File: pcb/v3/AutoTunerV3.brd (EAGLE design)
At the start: 100 x 80 mm, 113 parts, among them IC2 317EMP, Q1 32,768kHz, Q2 BSS123, Q3 BSS84, U1 TPS63070RNMR, Y1 8MHz

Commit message: board v3 improvements
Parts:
- added D1: (no value), diode:SOD323-R
- R32: value 100 -> 60
- moved T1 3.91 mm to (41.7, 55.8), turned to 0 degrees
- moved R28 3.25 mm to (44.7, 55.7), turned to 270 degrees
- moved ST_LINK 1.27 mm to (97.6, 56.4)
- moved +5V 0.95 mm to (33.6, 59.2)
- moved BUZZER 0.95 mm to (41.0, 47.1)
- moved JP2 0.95 mm to (97.6, 68.1)
- moved C10 0.64 mm to (55.3, 59.4)
- moved C11 0.64 mm to (55.3, 53.1)
- moved R37 0.64 mm to (54.3, 56.3)
- moved Q1 0.63 mm to (56.5, 56.3)
- moved R34 0.58 mm to (36.4, 56.0), turned to 90 degrees
- moved VBAT 0.32 mm to (7.60, 68.4)
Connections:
- net N$54: now also D1.A
- net N$55: now also D1.C
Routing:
- net GND: track 325.5 -> 340.0 mm, vias 16 -> 21
- net N$54: track 7.12 -> 13.5 mm
- net BUZZER: track 35.3 -> 29.3 mm
- net +3V3: track 170.2 -> 173.7 mm
- net N$55: track 7.98 -> 10.2 mm
- net N$56: track 4.19 -> 2.06 mm
- net +5V: track 26.8 -> 25.4 mm
- net SWDIO: track 22.5 -> 23.7 mm
- net SWDCLK: track 24.3 -> 25.6 mm
- net N$50: track 20.1 -> 21.0 mm
- net N$49: track 22.5 -> 23.5 mm
- net N$48: track 25.4 -> 26.4 mm
- net N$39: track 27.6 -> 28.5 mm
- net OSC32OUT: track 10.7 -> 11.3 mm
- net OSC32IN: track 12.7 -> 12.2 mm
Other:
- board text added: "+ -"
- board text added: "+3V3"
- board text added: "+5V"
- board text added: "BuildInLED"
- board text added: "Extenions"
- board text added: "GND"
- board text added: "Input"
- board text added: "SIGNAL_IN"
- board text added: "SIGNAL_OPAMP"
- board text added: "VBAT"
- board text added: "VBUS"
- board text added: "microcontroller"
- board text removed: "-"
- board text removed: "A_IN"
- board text removed: "PC13"
- board text removed: "uC"

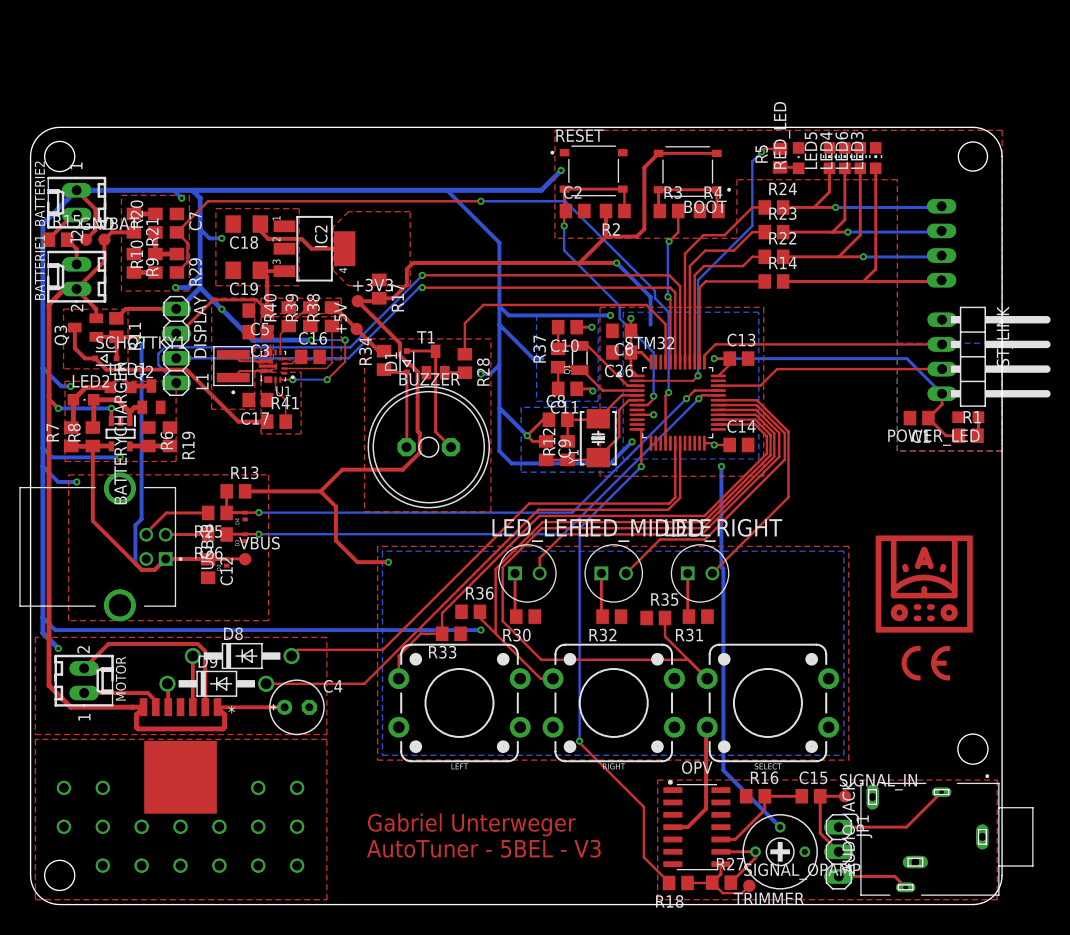
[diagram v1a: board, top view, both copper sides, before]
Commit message: board v3 dcdc design change
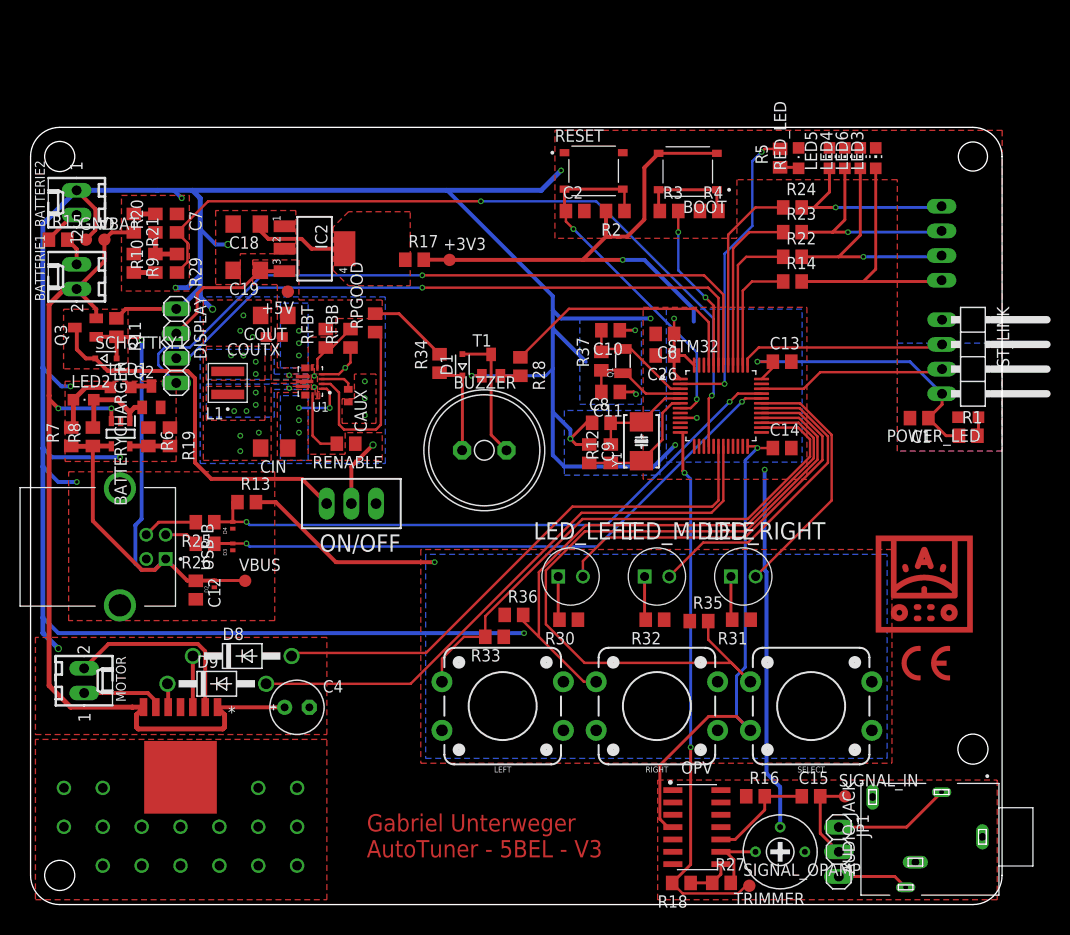
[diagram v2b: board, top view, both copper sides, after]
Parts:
- removed C16: 100n, rcl:C0805
- removed C17, C5: 47u, rcl:C0805
- removed C3: 10u, rcl:C0805
- removed R38, R39: 100k, rcl:R0805
- removed R40: 523k, rcl:R0805
- removed R41: 10k, rcl:R0805
- added CAUX: 100n, rcl:C0402
- added CIN, COUT: 47u, rcl:C1206
- added COUTX: 10u, rcl:C0603
- added ON/OFF: (no value), switch:TL3XPO
- added RENABLE: 10k, rcl:R0805
- added RFBB, RPGOOD: 100k, rcl:R0805
- added RFBT: 523k, rcl:R0805
- moved +3V3 10.4 mm to (43.1, 66.4)
- moved +5V 8.06 mm to (26.5, 63.1), turned to 180 degrees
- moved D1 5.72 mm to (44.5, 55.6)
- moved BUZZER 5.72 mm to (46.7, 46.8)
- moved R28 5.72 mm to (50.4, 55.4)
- moved R34 5.72 mm to (42.1, 55.7)
- moved T1 5.72 mm to (47.4, 55.5)
- moved R17 4.72 mm to (39.5, 66.4), turned to 0 degrees
- moved C26 4.46 mm to (65.3, 56.5)
- moved C6 4.46 mm to (65.3, 58.7)
- moved R35 4.46 mm to (68.8, 29.2)
- moved STM32 4.46 mm to (71.1, 51.3)
- moved C13 4.46 mm to (77.4, 55.9)
- moved C14 4.46 mm to (77.4, 47.0)
- moved C10 4.46 mm to (59.7, 59.1)
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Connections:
- net N$58 renamed L2
- net N$59 renamed L1
- removed net N$45: R18.2, STM32.12
- new net N$3: ON/OFF.3, Q3.3, SCHOTTKY1.C
- new net N$7: OPV.8, R18.1, R27.1
- net +5V: now also COUT.1, COUTX.1, RFBT.2, RPGOOD.2; no longer C3.1, C5.1, R38.2, R40.2
- net GND: now also CAUX.2, CIN.2, COUT.2, COUTX.2, RFBB.1; no longer C16.2, C17.2, C3.2, C5.2, R39.1
- net N$60: now also CAUX.1; no longer C16.1
- net N$61: now also RPGOOD.1; no longer R38.1
- net N$62: now also RFBB.2, RFBT.1; no longer R39.2, R40.1
- net N$64: now also RENABLE.2; no longer R41.2
- net SIGNAL_OPAMP: now also R18.2, STM32.12; no longer OPV.8, R18.1, R27.1
- net VIN: now also CIN.1, ON/OFF.2, RENABLE.1; no longer C17.1, Q3.3, R41.1, SCHOTTKY1.C
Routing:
- net N$45: track 53.6 -> 0.00 mm, vias 2 -> 0
- net SIGNAL_OPAMP: track 9.41 -> 56.5 mm, vias 0 -> 2
- net N$3: track 0.00 -> 39.7 mm
- net VIN: track 25.1 -> 12.8 mm, vias 0 -> 5
- net N$61: track 8.93 -> 20.0 mm
- net GND: track 340.0 -> 330.2 mm, vias 21 -> 29
- net USB+: track 58.0 -> 64.6 mm
- net USB-: track 56.5 -> 62.8 mm
- net N$7: track 0.00 -> 4.53 mm
- net DISPLAY_SDA: track 61.7 -> 66.2 mm
- net SWDCLK: track 25.6 -> 21.3 mm
- net MOTOR_PWM2: track 56.2 -> 60.5 mm
- net SWDIO: track 23.7 -> 19.4 mm
- net MOTOR_PWM1: track 51.8 -> 56.1 mm
- net DISPLAY_SCL: track 69.1 -> 73.4 mm
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- added copper zone on layer 16, net +5V
- added copper zone on layer 1, net L1
- added copper zone on layer 16, net L1
- added copper zone on layer 1, net L2
- added copper zone on layer 16, net L2
- added copper zone on layer 16, net VIN
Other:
- board text removed: "DCDC"

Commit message: board v3 finished
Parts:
- removed LED5, LED6: (no value), led:CHIP-LED0805
- added LED_CHARGE_GREEN, LED_CHARGE_RED: (no value), led:CHIPLED_0805
- LED1, LED2: device led:CHIPLED_0805 -> led:CHIP-LED0805
- R32: value 60 -> 56
- moved LED2 83.7 mm to (85.4, 76.8), turned to 0 degrees
- moved LED1 81.2 mm to (87.0, 76.8), turned to 0 degrees
- moved LED3 3.18 mm to (83.8, 76.8)
- moved LED4 1.59 mm to (82.2, 76.8)
- moved VBAT 0.32 mm to (7.92, 68.4)
- moved BATTERIE1 0.32 mm to (5.06, 64.6)
- moved BATTERIE2 0.32 mm to (5.06, 72.2)
- moved GND 0.32 mm to (6.01, 68.4)
- moved R15 0.32 mm to (3.15, 68.4)
- renumbered C4 to C_H-BRIDGE, D8 to D_H-BRIDGE1, D9 to D_H-BRIDGE2, JP2 to EXTENSIONS, Q1 to QUARTZ2, Q2 to N-CHANNEL, Q3 to P-CHANNEL, RED_LED to LED_INDICATOR, T1 to NPN, Y1 to QUARTZ
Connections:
- net GND: now also LED1.C, LED2.C; no longer LED5.C, LED6.C
- net N$11: now also LED_CHARGE_GREEN.A, LED_CHARGE_RED.A; no longer LED1.A, LED2.A
- net N$12: now also LED_CHARGE_GREEN.C; no longer LED1.C
- net N$39: now also LED1.A; no longer LED3.A
- net N$48: now also LED2.A; no longer LED6.A
- net N$49: now also LED3.A; no longer LED4.A
- net N$50: now also LED4.A; no longer LED5.A
- net N$9: now also LED_CHARGE_RED.C; no longer LED2.C
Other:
- board text added: "AutoTuner V3 - Maturaprojekt Gabriel Unterweger - 5BEL TFO Meran 23 / 24"
- board text removed: "Gabriel Unterweger AutoTuner - 5BEL - V3"

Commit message: settings menu
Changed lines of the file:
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@@
 <drawing>
 <settings>
-<setting alwaysvectorfont="yes"/>
+<setting alwaysvectorfont="no"/>
 <setting verticaltext="up"/>
 </settings>
@@
 <attribute name="VALUE" x="79.675" y="11.035" size="1.27" layer="27" rot="R180"/>
 </element>
-<element name="JP1" library="pinhead" library_urn="urn:adsk.eagle:library:325" package="1X03" package3d_urn="urn:adsk.eagle:package:22458/2" value="" x="83.1925" y="5.43" smashed="yes" rot="R270">
-<attribute name="NAME" x="85.0213" y="9.3162" size="1.27" layer="25" ratio="10" rot="R270"/>
-<attribute name="POPULARITY" value="92" x="83.1925" y="5.43" size="1.778" layer="27" rot="R270" display="off"/>
-<attribute name="VALUE" x="80.0175" y="9.24" size="1.27" layer="27" rot="R270"/>
-</element>
 <element name="LED1" library="led" library_urn="urn:adsk.eagle:library:259" package="CHIP-LED0805" package3d_urn="urn:adsk.eagle:package:15818/2" value="" x="86.995" y="76.835" smashed="yes">
 <attribute name="LCSC_PART" value="C2297" x="86.995" y="76.835" size="1.778" layer="27" display="off"/>
@@
 <attribute name="VALUE" x="25.7175" y="60.325" size="1.27" layer="27" rot="R180"/>
 </element>
+<element name="JP1" library="pinhead" library_urn="urn:adsk.eagle:library:325" package="1X03" package3d_urn="urn:adsk.eagle:package:22458/2" value="" x="83.185" y="5.3975" smashed="yes" rot="R270">
+<attribute name="NAME" x="85.0138" y="9.2837" size="1.27" layer="25" ratio="10" rot="R270"/>
+<attribute name="POPULARITY" value="92" x="83.185" y="5.3975" size="1.778" layer="27" rot="R270" display="off"/>
+<attribute name="VALUE" x="80.01" y="9.2075" size="1.27" layer="27" rot="R270"/>
+</element>
 </elements>
 <signals>
@@
 <signal name="N$11">
 <contactref element="LED_CHARGE_GREEN" pad="A"/>
-<contactref element="LED_CHARGE_RED" pad="A"/>
 <contactref element="R7" pad="2"/>
-<wire x1="4.1875" y1="49.1" x2="4.4075" y2="49.32" width="0.508" layer="1"/>
+<wire x1="8.2175" y1="53.23" x2="5.6775" y2="53.23" width="0.508" layer="1"/>
+<contactref element="LED_CHARGE_RED" pad="A"/>
+<wire x1="5.6775" y1="53.23" x2="4.4075" y2="51.96" width="0.508" layer="1"/>
 <wire x1="4.4075" y1="51.96" x2="4.4075" y2="49.32" width="0.508" layer="1"/>
-<wire x1="4.4075" y1="51.96" x2="5.6775" y2="53.23" width="0.508" layer="1"/>
-<wire x1="5.6775" y1="53.23" x2="8.2175" y2="53.23" width="0.508" layer="1"/>
+<wire x1="4.4075" y1="49.32" x2="4.1875" y2="49.1" width="0.508" layer="1"/>
 </signal>
 <signal name="N$9">
@@
 <contactref element="AUDIO_JACK" pad="5"/>
 <contactref element="JP1" pad="1"/>
-<wire x1="93.775" y1="11.57" x2="90.175" y2="7.97" width="0.3048" layer="1"/>
-<wire x1="90.175" y1="7.97" x2="83.1925" y2="7.97" width="0.3048" layer="1"/>
+<wire x1="90.1425" y1="7.9375" x2="83.185" y2="7.9375" width="0.3048" layer="1"/>
+<wire x1="93.775" y1="11.57" x2="90.1425" y2="7.9375" width="0.3048" layer="1"/>
 </signal>
 <signal name="SIGNAL_IN_2">
 <contactref element="AUDIO_JACK" pad="2"/>
 <contactref element="JP1" pad="3"/>
-<wire x1="83.1925" y1="2.89" x2="88.955" y2="2.89" width="0.3048" layer="1"/>
-<wire x1="88.955" y1="2.89" x2="90.075" y2="1.77" width="0.3048" layer="1"/>
+<wire x1="90.075" y1="1.77" x2="88.9875" y2="2.8575" width="0.3048" layer="1"/>
+<wire x1="88.9875" y1="2.8575" x2="83.185" y2="2.8575" width="0.3048" layer="1"/>
 </signal>
 <signal name="SIGNAL_IN">
-<contactref element="JP1" pad="2"/>
 <contactref element="C15" pad="2"/>
 <contactref element="SIGNAL_IN" pad="TP"/>
-<wire x1="83.1925" y1="5.43" x2="81.285" y2="7.3375" width="0.3048" layer="1"/>
-<wire x1="81.285" y1="7.3375" x2="81.285" y2="11.145" width="0.3048" layer="1"/>
 <wire x1="83.8275" y1="11.145" x2="81.285" y2="11.145" width="0.3048" layer="1"/>
+<contactref element="JP1" pad="2"/>
+<wire x1="83.185" y1="5.3975" x2="81.285" y2="7.2975" width="0.3048" layer="1"/>
+<wire x1="81.285" y1="7.2975" x2="81.285" y2="11.145" width="0.3048" layer="1"/>
 </signal>
 <signal name="CUSTOM2">

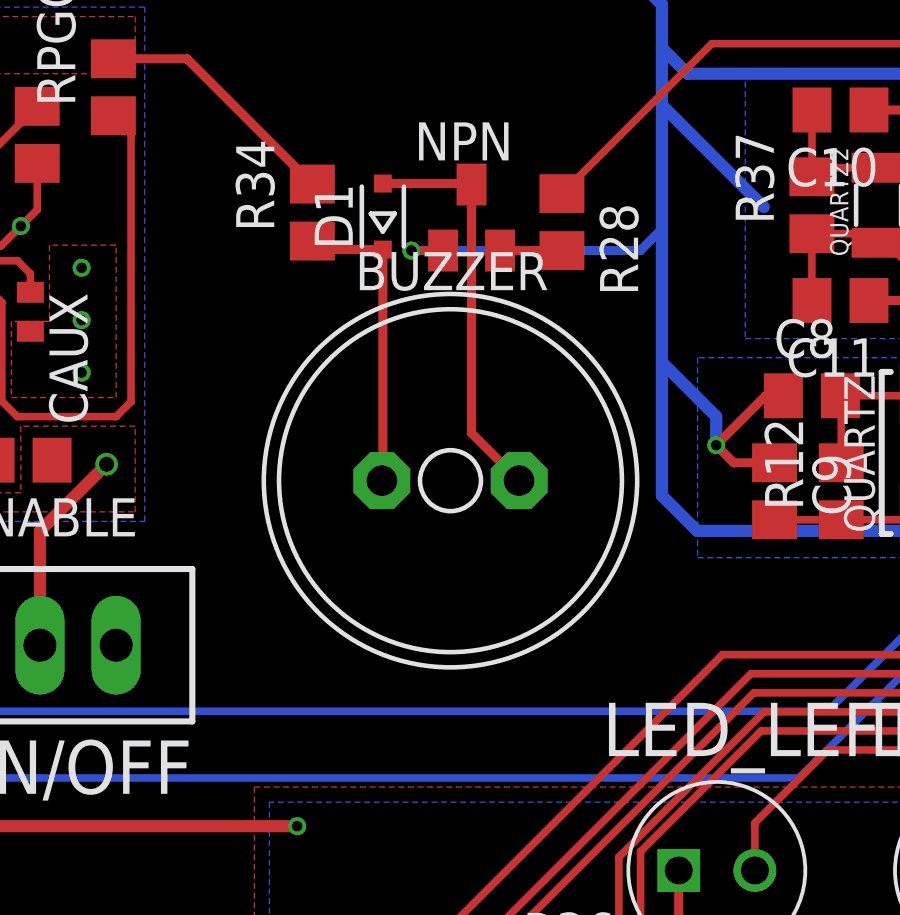
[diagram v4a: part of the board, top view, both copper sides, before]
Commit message: critical bat fault & buzzer
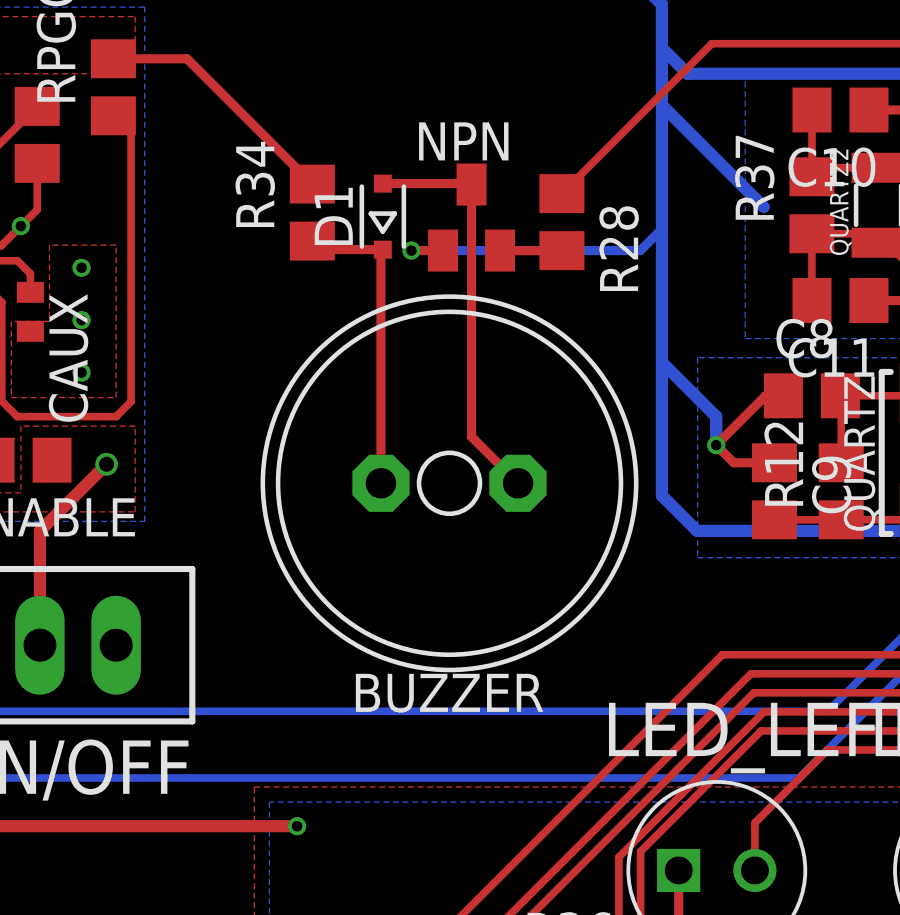
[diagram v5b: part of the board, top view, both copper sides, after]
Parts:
- R20: value 330k -> 820k
- R21: value 470k -> 1M
- R34: value 10k -> 0
- R9: value 1M -> 118k
- moved BUZZER 0.09 mm to (46.7, 46.7), turned to 180 degrees
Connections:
- net N$54: now also BUZZER.-; no longer BUZZER.+
- net N$55: now also BUZZER.+; no longer BUZZER.-
